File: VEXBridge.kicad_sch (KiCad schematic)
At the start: 58 parts, among them J1 4P4C, J10 QWIIC Connector, J11 QWIIC Connector, J12 QWIIC Connector, J13 QWIIC Connector, J14 QWIIC Connector, J2 Conn_01x04, J3 Conn_01x04, J4 QWIIC Connector, J5 QWIIC Connector, J6 Conn_01x04, J7 Conn_01x04, J8 USB_C_Receptacle_USB2.0_14P, J9 QWIIC Connector, U1 PCA9548ADB, U2 ESP32-S3-MINI-1U, U3 LSM9DS1, U4 AMS1117-3.3, U5 LM2595S-5

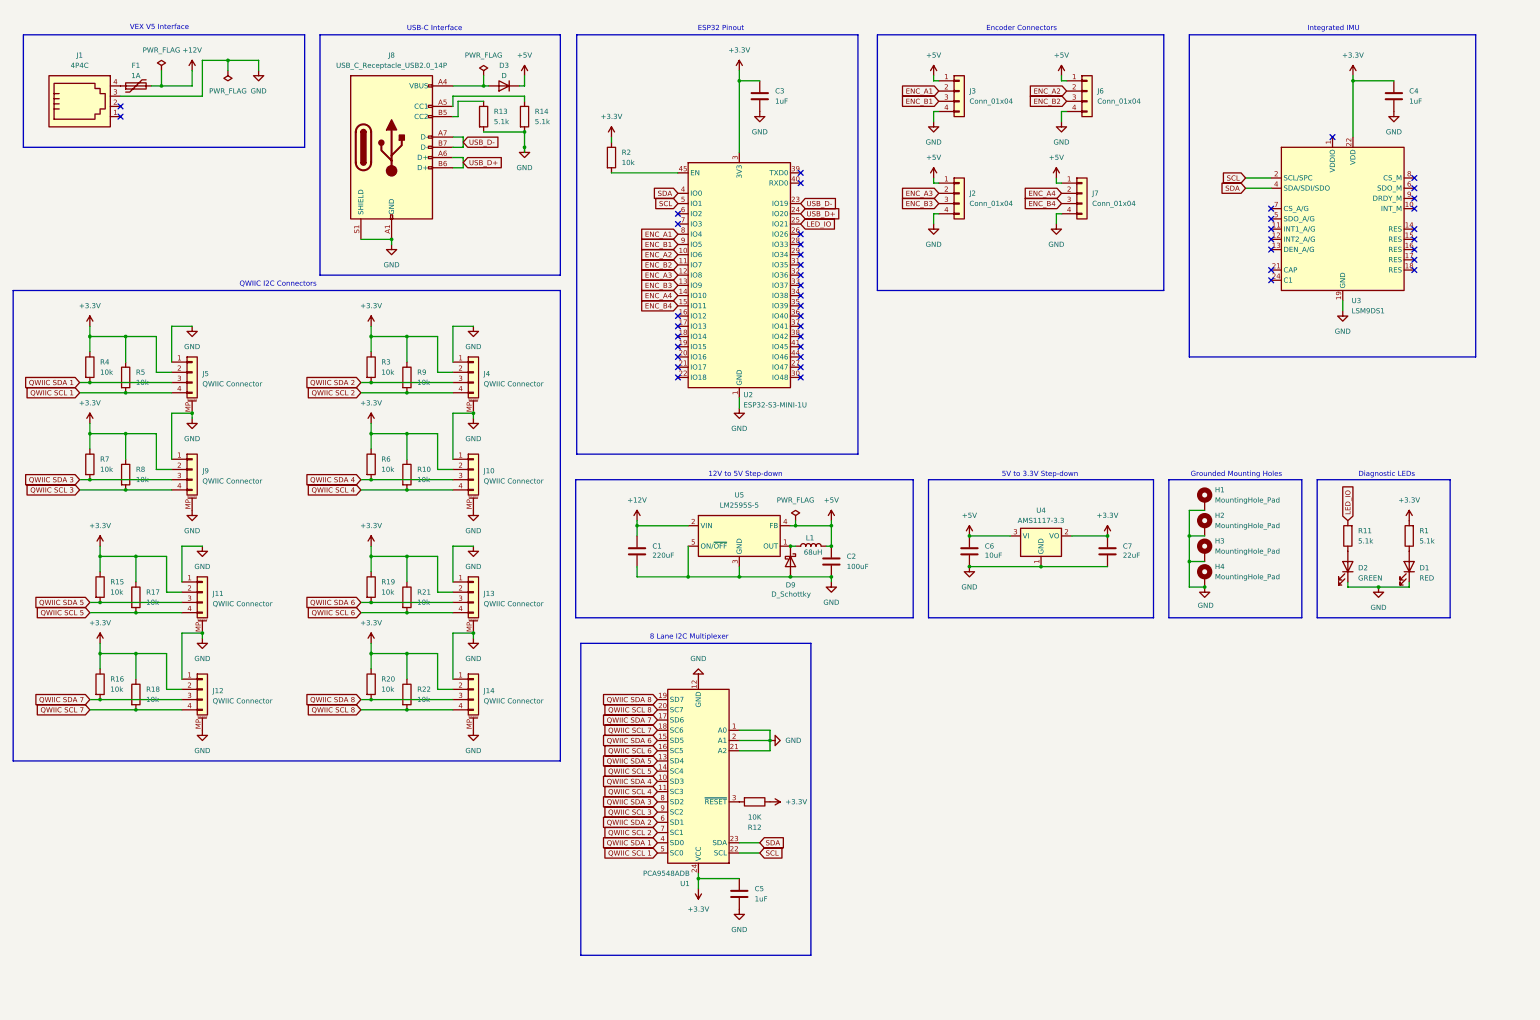
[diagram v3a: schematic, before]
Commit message: Bug Fixes for PCB Draft
- Replaced LEDs with a single RGB LED
- Routed 4 QWIIC connectors directly to ESP32 instead of multiplexer
- Replaced IMU and added IMU address jumper
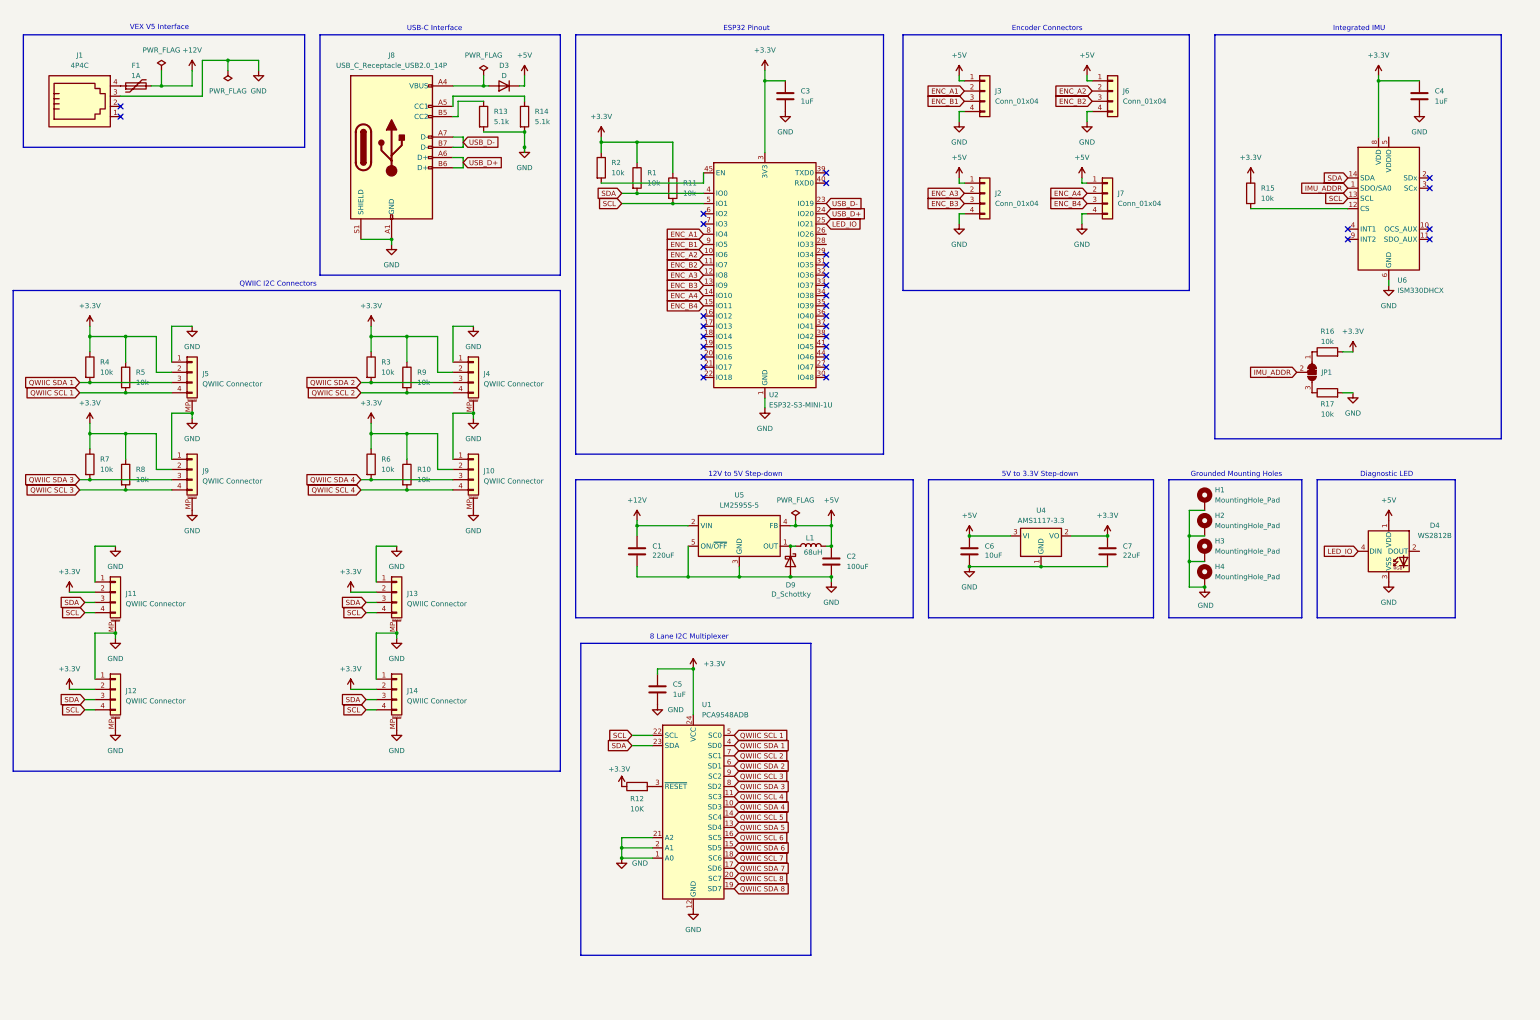
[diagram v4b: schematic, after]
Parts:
- removed D1: RED, LED_SMD:LED_0603_1608Metric, symbol Device:LED
- removed D2: GREEN, LED_SMD:LED_0603_1608Metric, symbol Device:LED
- removed R18, R19, R20, R21, R22: 10k, Resistor_SMD:R_0805_2012Metric, symbol Device:R
- removed U3: LSM9DS1, Package_LGA:LGA-24L_3x3.5mm_P0.43mm, symbol Sensor_Motion:LSM9DS1
- added D4: WS2812B, LED_SMD:LED_WS2812B_PLCC4_5.0x5.0mm_P3.2mm, symbol LED:WS2812B
- added JP1: SolderJumper_3_Bridged12, symbol Jumper:SolderJumper_3_Bridged12
- added U6: ISM330DHCX, Package_LGA:LGA-14_3x2.5mm_P0.5mm_LayoutBorder3x4y, symbol Sensor_Motion:ISM330DHCX
- R1, R11: value 5.1k -> 10k
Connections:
- net +3.3V: now also R1.1, R11.1, R16.2, U6.8 (VDD); no longer R1.2, R16.1, R17.1
- net +5V: now also D4.1 (VDD)
- net GND: now also R17.2, D4.3 (VSS), U6.6 (GND), U6.7 (GND)
- net LED_IO: now also D4.4 (DIN); no longer R11.2
- net QWIIC SCL 5: no longer J11.4 (Pin_4), R17.2
- net QWIIC SCL 6: no longer J13.4 (Pin_4)
- net QWIIC SCL 7: no longer J12.4 (Pin_4)
- net QWIIC SCL 8: no longer J14.4 (Pin_4)
- net QWIIC SDA 5: no longer J11.3 (Pin_3), R15.2
- net QWIIC SDA 6: no longer J13.3 (Pin_3)
- net QWIIC SDA 7: no longer J12.3 (Pin_3), R16.2
- net QWIIC SDA 8: no longer J14.3 (Pin_3)
- net SCL: now also J11.4 (Pin_4), J12.4 (Pin_4), J13.4 (Pin_4), J14.4 (Pin_4), R11.2, U6.13 (SCL)
- net SDA: now also J11.3 (Pin_3), J12.3 (Pin_3), J13.3 (Pin_3), J14.3 (Pin_3), R1.2, U6.14 (SDA)
- new net: JP1.1 (A), R16.1
- new net: JP1.3 (B), R17.1
- new net: R15.2, U6.12 (CS)
- new net IMU_ADDR: JP1.2 (C), U6.1 (SDO/SA0)
- no-connect marks 45 -> 32
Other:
- note added: "Diagnostic LED"
- note removed: "Diagnostic LEDs"
- moved on the sheet: C3, C4, C5, J11, J12, J2, J3, J6, J7, R12, R2, U1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

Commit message: I have no idea what I did
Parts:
- added C8: 1uF, Capacitor_SMD:C_0201_0603Metric, symbol Device:C
- added D6: ESDLC5V0PB8, Package_DFN_QFN:UDFN-9_1.0x3.8mm_P0.5mm, symbol Power_Protection:ESDLC5V0PB8
- added J15: 4P4C, Connector_RJ:RJ9_Evercom_5301-440xxx_Horizontal, symbol Connector:4P4C
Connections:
- net +12V: now also J15.4
- net +3.3V: now also U6.5 (VDDIO), C8.1, D6.4 (K3)
- net +5V: now also D6.5 (K4)
- net GND: now also U6.2 (SDx), U6.3 (SCx), C8.2, D6.3 (A), J15.3
- net SCL: now also D6.1 (K1)
- net SDA: now also D6.2 (K2)
- net USB_D+: now also D6.9 (K8)
- net USB_D-: now also D6.8 (K7)
- net B: now reaches J1.1
- net B: now also D6.7 (K6), J15.1
- net A: now reaches J1.2
- net A: now also D6.6 (K5), J15.2
- no-connect marks 32 -> 29
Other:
- note added: "ESD Protection"
- moved on the sheet: C4

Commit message: Completed schematic
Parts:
- removed C8: 1uF, Capacitor_SMD:C_0201_0603Metric, symbol Device:C
- removed D4: WS2812B, LED_SMD:LED_WS2812B_PLCC4_5.0x5.0mm_P3.2mm, symbol LED:WS2812B
- removed D6: ESDLC5V0PB8, Package_DFN_QFN:UDFN-9_1.0x3.8mm_P0.5mm, symbol Power_Protection:ESDLC5V0PB8
- removed D9: D_Schottky, Diode_SMD:D_SMA, symbol Device:D_Schottky
- removed J10, J11, J12, J13, J14, J4, J5, J9: QWIIC Connector, Connector_JST:JST_SH_SM04B-SRSS-TB_1x04-1MP_P1.00mm_Horizontal, symbol Connector_Generic_MountingPin:Conn_01x04_MountingPin
- removed J15: 4P4C, Connector_RJ:RJ9_Evercom_5301-440xxx_Horizontal, symbol Connector:4P4C
- removed JP1: SolderJumper_3_Bridged12, symbol Jumper:SolderJumper_3_Bridged12
- removed R6: 10k, Resistor_SMD:R_0805_2012Metric, symbol Device:R
- removed U5: LM2595S-5, Package_TO_SOT_SMD:TO-263-5_TabPin3, symbol Regulator_Switching:LM2595S-5
- removed U6: ISM330DHCX, Package_LGA:LGA-14_3x2.5mm_P0.5mm_LayoutBorder3x4y, symbol Sensor_Motion:ISM330DHCX
- added C10: 1uF, Capacitor_SMD:C_1210_3225Metric, symbol Device:C
- added C13, C15: 1uF, Capacitor_SMD:C_0201_0603Metric, symbol Device:C
- added C14: 22uF, Capacitor_SMD:C_0201_0603Metric, symbol Device:C
- added C3: 220nF, Capacitor_SMD:C_1210_3225Metric, symbol Device:C
- added C5, C6, C7: 22uF, Capacitor_SMD:C_1206_3216Metric, symbol Device:C
- added D1: D, Diode_SMD:D_0201_0603Metric, symbol Device:D
- added D3: RED, symbol Device:LED
- added D4: BLUE, symbol Device:LED
- added J10: Port 1, Connector_Molex:Molex_Mini-Fit_Jr_5569-04A2_2x02_P4.20mm_Horizontal, symbol Connector_Generic:Conn_02x02_Odd_Even
- added J11: Port 2, Connector_Molex:Molex_Mini-Fit_Jr_5569-04A2_2x02_P4.20mm_Horizontal, symbol Connector_Generic:Conn_02x02_Odd_Even
- added J12: Port 3, Connector_Molex:Molex_Mini-Fit_Jr_5569-04A2_2x02_P4.20mm_Horizontal, symbol Connector_Generic:Conn_02x02_Odd_Even
- added J13: Port 4, Connector_Molex:Molex_Mini-Fit_Jr_5569-04A2_2x02_P4.20mm_Horizontal, symbol Connector_Generic:Conn_02x02_Odd_Even
- added J4: Port C, Connector_JST:JST_SH_SM04B-SRSS-TB_1x04-1MP_P1.00mm_Horizontal, symbol Connector_Generic:Conn_01x04
- added J5: Port D, Connector_JST:JST_SH_SM04B-SRSS-TB_1x04-1MP_P1.00mm_Horizontal, symbol Connector_Generic:Conn_01x04
- added J8: Port G, Connector_JST:JST_SH_SM04B-SRSS-TB_1x04-1MP_P1.00mm_Horizontal, symbol Connector_Generic:Conn_01x04
- added J9: Port H, Connector_JST:JST_SH_SM04B-SRSS-TB_1x04-1MP_P1.00mm_Horizontal, symbol Connector_Generic:Conn_01x04
- added JP2: Multiplexer Addr, symbol Jumper:SolderJumper_3_Bridged12
- added Q1, Q2, Q3, Q4, Q5, Q6, Q7, Q8: BSS138, Package_TO_SOT_SMD:SOT-23, symbol Transistor_FET:BSS138
- added R12, R13, R14, R18, R19, R20, R21, R22, R23, R28, R29, R30, R31: 10k, Resistor_SMD:R_0805_2012Metric, symbol Device:R
- added R26: 4.7k, Resistor_SMD:R_0805_2012Metric, symbol Device:R
- added R27: 2.2k, Resistor_SMD:R_0805_2012Metric, symbol Device:R
- added SW1: Reset, symbol Switch:SW_SPST
- added SW2: Boot, symbol Switch:SW_SPST
- added U1: LMR33630ADDA, Package_SO:Texas_HSOP-8-1EP_3.9x4.9mm_P1.27mm_ThermalVias, symbol Regulator_Switching:LMR33630ADDA
- added U3: D3V3XA4B10LP, Package_DFN_QFN:Diodes_UDFN-10_1x2.5mm_P0.5mm, symbol Power_Protection:D3V3XA4B10LP
- added U7: MAX485E, Package_SO:SOIC-8_3.9x4.9mm_P1.27mm, symbol Interface_UART:MAX485E
- C1: value 220uF -> 0.1uF
- C12: renamed from C3; value 1uF -> 4.7uF
- C2: value 100uF -> 10uF; footprint Capacitor_SMD:C_1206_3216Metric -> Capacitor_SMD:C_1210_3225Metric
- C4: value 1uF -> 22uF; footprint Capacitor_SMD:C_0201_0603Metric -> Capacitor_SMD:C_1206_3216Metric
- F1: value 1A -> 2A
- J1: value 4P4C -> VEX V5
- J2: value Conn_01x04 -> Port A; footprint Connector_Molex:Molex_PicoBlade_53047-0410_1x04_P1.25mm_Vertical -> Connector_JST:JST_SH_SM04B-SRSS-TB_1x04-1MP_P1.00mm_Horizontal
- J3: value Conn_01x04 -> Port B; footprint Connector_Molex:Molex_PicoBlade_53047-0410_1x04_P1.25mm_Vertical -> Connector_JST:JST_SH_SM04B-SRSS-TB_1x04-1MP_P1.00mm_Horizontal
- J6: value Conn_01x04 -> Port E; footprint Connector_Molex:Molex_PicoBlade_53047-0410_1x04_P1.25mm_Vertical -> Connector_JST:JST_SH_SM04B-SRSS-TB_1x04-1MP_P1.00mm_Horizontal
- J7: value Conn_01x04 -> Port F; footprint Connector_Molex:Molex_PicoBlade_53047-0410_1x04_P1.25mm_Vertical -> Connector_JST:JST_SH_SM04B-SRSS-TB_1x04-1MP_P1.00mm_Horizontal
- L1: value 68uH -> 8uH; footprint Inductor_SMD:L_SXN_SMDRI127 -> Inductor_SMD:L_0603_1608Metric
- R1: value 10k -> 100k
- R2: value 10k -> 24.9k
- R3, R4: value 10k -> 2k
- R6: renamed from R12; footprint (none) -> Resistor_SMD:R_0805_2012Metric
- renumbered C5 to C11, C6 to C8, C7 to C9, D3 to D2, J8 to J14, R13 to R24, R14 to R25, U4 to U2, U1 to U4, U2 to U6
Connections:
- net QWIIC SDA 6 is gone; now on net SDA6: U4.15 (SD5)
- net +12V: now also C2.1, C3.1, U1.2 (VIN), U1.3 (EN); no longer C1.1
- net +3.3V: now also J2.3 (Pin_3), J3.3 (Pin_3), J6.3 (Pin_3), J7.3 (Pin_3), R16.1, R3.2, R4.2, C14.1, J4.3 (Pin_3), J5.3 (Pin_3), J8.3 (Pin_3), J9.3 (Pin_3), JP2.3 (B), Q1.1 (G), Q2.1 (G), Q3.1 (G), Q4.1 (G), Q5.1 (G), Q6.1 (G), Q7.1 (G), Q8.1 (G), R12.1, R14.1, R18.1, R20.1, R22.1, R26.1; no longer C4.1, R1.1, R11.1, R15.1, R16.2, R2.1, R3.1, R4.1, R7.1, R9.1
- net +5V: now also R11.2, R15.2, R17.2, R7.1, R9.2, C13.1, D1.1 (K), J10.1 (Pin_1), J11.1 (Pin_1), J12.1 (Pin_1), J13.1 (Pin_1), R13.2, R19.2, R21.2, R23.2, R28.1, R30.1, U7.8 (VCC); no longer C2.1, J2.1 (Pin_1), J3.1 (Pin_1), J6.1 (Pin_1), J7.1 (Pin_1), L1.2
- net A: now also R30.2, U3.1, U7.6 (A)
- net B: now also R31.1, U3.2, U7.7 (B)
- net GND: now also R2.2, U6.41 (IO45), U6.44 (IO46), C10.2, C13.2, C14.2, C15.2, C3.2, C5.2, C6.2, C7.2, D3.1 (K), D4.1 (K), J10.3 (Pin_3), J11.3 (Pin_3), J12.3 (Pin_3), J13.3 (Pin_3), J4.4 (Pin_4), J5.4 (Pin_4), J8.4 (Pin_4), J9.4 (Pin_4), JP2.1 (A), R29.2, R31.2, SW1.2 (B), SW2.2 (B), U1.1 (GND), U1.9 (GND), U3.3 (VSS), U3.8 (VSS), U7.5 (GND); no longer C1.2, R17.2, U4.21 (A2)
- net LED_IO: now also U6.16 (IO12), R27.1; no longer U6.25 (IO21)
- net SCL: now also R3.1, U6.15 (IO11); no longer R11.2, U6.5 (IO1)
- net SDA: now also R4.1, U6.14 (IO10); no longer R1.2, U6.4 (IO0)
- net USB_D+: now also U3.4
- net USB_D-: now also U3.5
- net at L1.1: now also C1.2, U1.8 (SW)
- net GPIO2_HV: now reaches R17.1
- net GPIO2_HV: now also J10.4 (Pin_4), Q5.3 (D)
- net RTS: now reaches U6.20 (IO16)
- net RTS: now also R29.1, U7.2 (~{RE}), U7.3 (DE)
- net TX: now reaches U6.21 (IO17)
- net TX: now also R28.2, U7.4 (DI)
- net RX: now reaches U6.22 (IO18)
- net RX: now also R7.2, U7.1 (RO)
- net ENABLE: now reaches U6.45 (EN)
- net ENABLE: now also R5.2, C15.1, SW1.1 (A); no longer R2.2
- net GPIO2: now reaches U6.6 (IO2)
- net GPIO2: now also R16.2, Q5.2 (S)
- net ENC_A1 renamed GPIO3
- net GPIO3: now also R10.2, Q2.2 (S); no longer J3.2 (Pin_2)
- net ENC_A2 renamed GPIO5
- net GPIO5: now also Q3.2 (S), R12.2; no longer J6.2 (Pin_2)
- net ENC_A3 renamed GPIO7
- net GPIO7: now also Q4.2 (S), R14.2; no longer J2.2 (Pin_2)
- net ENC_A4 renamed SDA6
- net SDA6: no longer U6.14 (IO10)
- net ENC_B1 renamed GPIO4
- net GPIO4: now also Q6.2 (S), R18.2; no longer J3.3 (Pin_3)
- net ENC_B2 renamed GPIO6
- net GPIO6: now also Q7.2 (S), R20.2; no longer J6.3 (Pin_3)
- net ENC_B3 renamed GPIO8
- net GPIO8: now also Q8.2 (S), R22.2; no longer J2.3 (Pin_3)
- removed net ENC_B4: J7.3 (Pin_3), U6.15 (IO11)
- net QWIIC SCL 1 renamed SCL1
- net SCL1: now also J2.1 (Pin_1); no longer R5.2
- net QWIIC SCL 2 renamed SCL2
- net SCL2: now also J3.1 (Pin_1); no longer R9.2
- net QWIIC SCL 3 renamed GPIO1
- net GPIO1: now also U6.5 (IO1), Q1.2 (S); no longer U4.9 (SC2)
- net QWIIC SCL 4 renamed SCL4
- net SCL4: now also J5.1 (Pin_1); no longer R10.2
- net QWIIC SCL 5 renamed SCL5
- net SCL5: now also J6.1 (Pin_1)
- net QWIIC SCL 6 renamed SCL6
- net SCL6: now also J7.1 (Pin_1)
- net QWIIC SCL 7 renamed SCL7
- net SCL7: now also J8.1 (Pin_1)
- net QWIIC SCL 8 renamed SCL8
- net SCL8: now also J9.1 (Pin_1)
- net QWIIC SDA 1 renamed SDA1
- net SDA1: now also J2.2 (Pin_2); no longer R4.2
- net QWIIC SDA 2 renamed SDA2
- net SDA2: now also J3.2 (Pin_2); no longer R3.2
- net QWIIC SDA 3 renamed SDA3
- net SDA3: now also J4.2 (Pin_2); no longer R7.2
- net QWIIC SDA 4 renamed SDA4
- net SDA4: now also J5.2 (Pin_2)
- net QWIIC SDA 5 renamed SDA5
- net SDA5: now also J6.2 (Pin_2)
- net QWIIC SDA 7 renamed SDA7
- net SDA7: now also J8.2 (Pin_2)
- net QWIIC SDA 8 renamed SDA8
- net SDA8: now also J9.2 (Pin_2)
- new net: C4.1, C5.1, C6.1, C7.1, D1.2 (A), L1.2, R1.1
- new net: D4.2 (A), R27.2
- new net: D3.2 (A), R26.2
- new net: R1.2, R2.1, U1.5 (FB)
- new net: C10.1, U1.6 (VCC)
- new net: C1.1, U1.7 (BOOT)
- new net BOOT: SW2.1 (A), U6.4 (IO0)
- new net GPIO1_HV: J10.2 (Pin_2), Q1.3 (D), R9.1
- new net GPIO3_HV: J11.2 (Pin_2), Q2.3 (D), R11.1
- new net GPIO4_HV: J11.4 (Pin_4), Q6.3 (D), R19.1
- new net GPIO5_HV: J12.2 (Pin_2), Q3.3 (D), R13.1
- new net GPIO6_HV: J12.4 (Pin_4), Q7.3 (D), R21.1
- new net GPIO7_HV: J13.2 (Pin_2), Q4.3 (D), R15.1
- new net GPIO8_HV: J13.4 (Pin_4), Q8.3 (D), R23.1
- new net Multi_ADDR: JP2.2 (C), U4.21 (A2)
- new net SCL3: J4.1 (Pin_1), U4.9 (SC2)
- no-connect marks 29 -> 25
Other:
- note added: "3.3V - 5V Logic Level Shifters"
- note added: "Boot Control"
- note added: "Diagnostic LEDs"
- note added: "GPIO Ports"
- note added: "I2C Address"
- note added: "I2C Ports"
- note added: "JTAG"
- note added: "RS-485 to RS-232"
- note added: "SPI0"
- note added: "UART0"
- note removed: "Diagnostic LED"
- note removed: "Encoder Connectors"
- note removed: "Integrated IMU"
- note removed: "QWIIC I2C Connectors"
- moved on the sheet: C11, C12, C8, C9, D2, F1, H1, H2, H3, H4, J1, J14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
